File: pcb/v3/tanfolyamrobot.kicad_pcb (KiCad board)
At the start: 2 copper layers, 95.9 x 61.6 mm, 78 parts, among them M1 DRV8833, Q1 BSO201SP, Q2 BSS123, Q3 BSS123, Q4 BSS123, SW1 SW_DPDT_x2, U1 STM32F411RCTx, U2 LP2950?CDT, U4 FT232RL, U5 LD117A?S, X1 MURATA_CSTCE, X2 1751248, X6 KUSBVX-BS1N

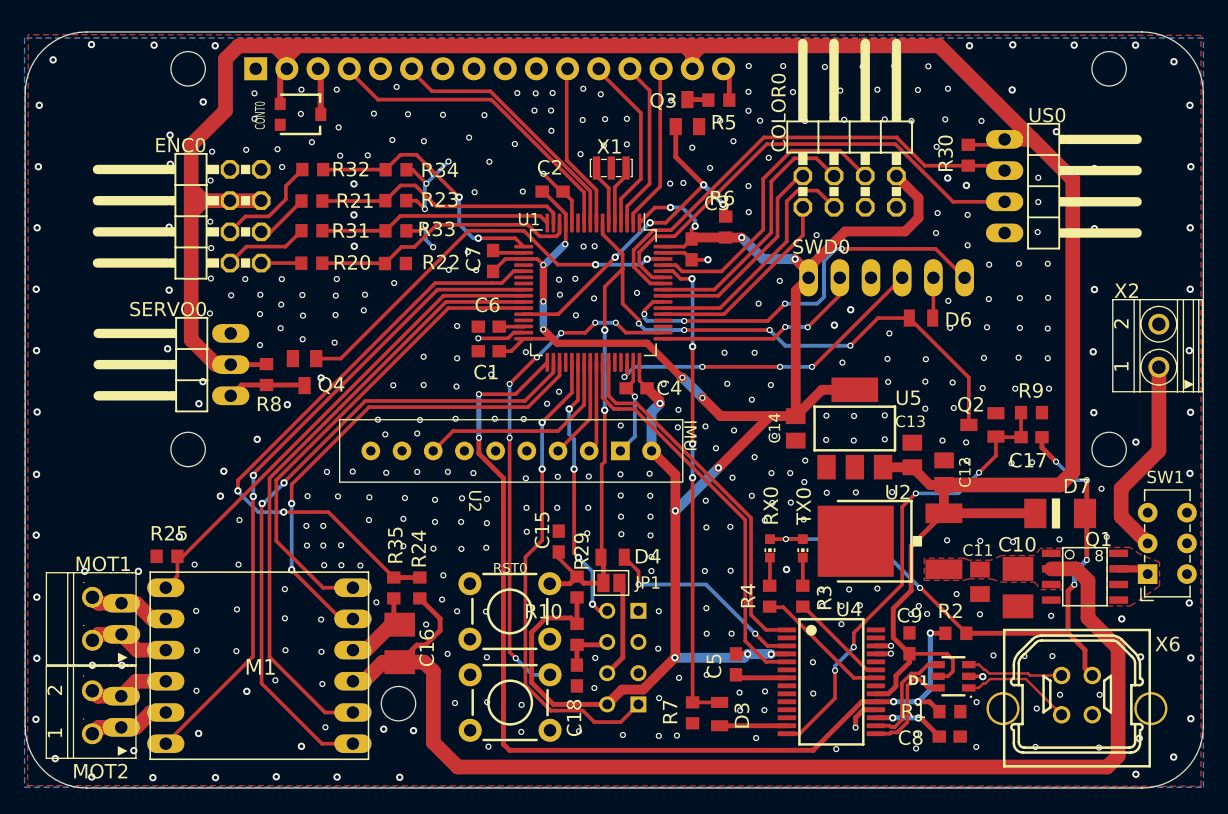
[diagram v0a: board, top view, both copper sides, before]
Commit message: Fixed some pcb errors
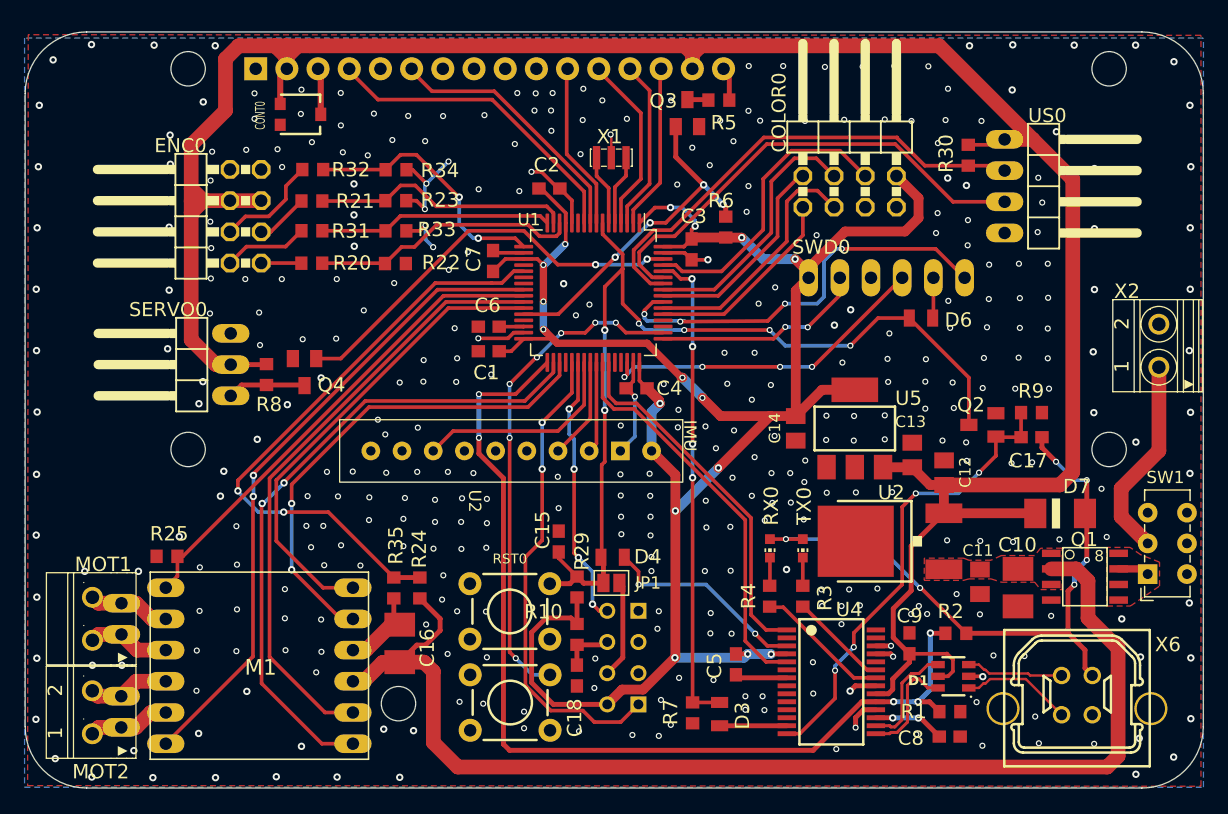
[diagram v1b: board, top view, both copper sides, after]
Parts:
- moved X1 0.84 mm to (102.3, 69.9)
- moved C2 0.36 mm to (97.2, 72.4)
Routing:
- net GND: track 53.7 -> 59.2 mm, vias 425 -> 375
- net /SWD_SWO: track 33.8 -> 34.4 mm

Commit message: Fixed DRC
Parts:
- moved C7 0.28 mm to (92.4, 78.3)
- moved C2 0.21 mm to (97.1, 72.3)
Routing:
- net GND: track 59.2 -> 86.6 mm, vias 375 -> 376
- net +3V3: track 172.7 -> 175.2 mm
- net /MOTOR1_IN1: track 53.1 -> 53.8 mm

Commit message: Finishing touches
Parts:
- added C20: 4u7, tanfolyamrobot:C0603, F.Cu at (106.9, 87.7)
- added C21: 100n, tanfolyamrobot:C0603, F.Cu at (82.1, 80.9)
- added C22: 10u, tanfolyamrobot:C0805K, F.Cu at (93.6, 71.4)
- added C23: 10u, tanfolyamrobot:C0805K, F.Cu at (90.0, 67.7)
- added C24: 100n, tanfolyamrobot:C0603, F.Cu at (97.0, 72.3)
- added C25: 68u, tanfolyamrobot:B_3528-21R, F.Cu at (138.3, 86.2)
- added C26: 68u, tanfolyamrobot:B_3528-21R, F.Cu at (117.1, 92.5)
- added FB1: 220, Inductor_SMD:L_0603_1608Metric, F.Cu at (92.5, 68.9)
- added G***: LOGO, tanfolyamrobot:LEGO, B.Cu at (92.7, 73.7)
- added R13: 10K, tanfolyamrobot:R0603, F.Cu at (95.3, 99.7)
- added R14: 4K7, tanfolyamrobot:R0603, F.Cu at (79.3, 81.4)
- D3, D4, D6: footprint tanfolyamrobot:MICROMELF-W -> Diode_SMD:D_SOD-323F
- RX0, TX0: footprint tanfolyamrobot:CHIP-LED0603 -> LED_SMD:LED_0603_1608Metric
- moved R35 25.3 mm to (76.5, 81.0), turned to 90 degrees
- moved R24 23.3 mm to (77.5, 83.5), turned to 180 degrees
- moved C2 9.29 mm to (106.3, 73.3), turned to 45 degrees
- moved C14 2.94 mm to (114.4, 92.0)
- moved C9 1.24 mm to (125.7, 110.3)
- moved D6 0.35 mm to (127.6, 83.3)
- turned RX0 to 90 degrees
- turned TX0 to 90 degrees
- renumbered U2 to IC2, U4 to IC4, U5 to IC5
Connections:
- IC4 pad 13: /FTDI_BOOT0_OUT -> /FTDI_CBUS2
- IC4 pad 3: /FTDI_RSTN_OUT -> /FTDI_RTSN
- U1 pad 13: +3V3 -> Net-(U1-VDDA)
- U1 pad 21: /VCC_SENSE -> /VCC_SENSE_FILTERED
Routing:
- net /VCC_SENSE: track 49.2 -> 3.89 mm, vias 2 -> 0
- net VCC: track 96.6 -> 134.7 mm, vias 0 -> 4
- net /FTDI_RTSN: track 0.00 -> 16.5 mm, vias 0 -> 2
- net /FTDI_RSTN_OUT: track 16.5 -> 0.00 mm, vias 2 -> 0
- net /VCC_SENSE_FILTERED: track 0.00 -> 16.2 mm, vias 0 -> 2
- net +3V3: track 175.2 -> 191.4 mm, vias 16 -> 18
- net GND: track 86.6 -> 98.4 mm, vias 376 -> 367
- net Net-(U1-VDDA): track 0.00 -> 9.26 mm
- net /FTDI_CBUS2: track 0.00 -> 5.48 mm
- net /FTDI_BOOT0_OUT: track 5.48 -> 0.00 mm
- net /MOTOR_FAULTN: track 53.4 -> 55.7 mm
- net /BUTTON: track 40.9 -> 42.4 mm, vias 7 -> 5
- net /TAVMERO_SCL: track 39.5 -> 40.9 mm
- net /USB-: track 7.93 -> 9.03 mm
- net /USB_INTERNAL-: track 8.96 -> 9.62 mm
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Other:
- board text added: "+"
- board text added: "-"
- board text added: "3V3"
- board text added: "3V3 SCK GND SIO NRS SWO"
- board text added: "5V ECH TRIG GND"
- board text added: "COLOR_S0 COLOR_S3 COLOR_S1 COLOR_S2 GND COLOR_OU GND 3V3"
- board text added: "GND"
- board text added: "GND 5V PWM"
- board text added: "GND GND 5V 5V ENC2B ENC1B ENC2A ENC1A"
- board text added: "IN4 IN3 GND VCC IN2 IN1"
- board text added: "INT"
- board text added: "NSLP OUT1 OUT2 OUT3 OUT4 NFLT"
- board text added: "SCL"
- board text added: "SDA"
- board text added: "Tanfolyamrobot v3.0 Designed by: Fiák Ádám"
- board text added: "VCC"
